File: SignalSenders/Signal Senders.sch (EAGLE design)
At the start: 14 parts, among them IC2 MEGA8-P

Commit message: add reset switch, add power input capacitor
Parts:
- added C3: 22pF, rcl:C-USC0805
- added S1: (no value), SparkFun-Electromechanical:TAC_SWITCHPTH
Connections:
- new net N$1: IC2.PC6(/RESET), S1.4
- net +5V: now also C3.1
- net GND: now also C3.2, S1.2
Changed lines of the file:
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@@
 <layer number="106" name="bPlate" color="7" fill="1" visible="no" active="yes"/>
 <layer number="107" name="Crop" color="7" fill="1" visible="no" active="yes"/>
+<layer number="108" name="tplace-old" color="10" fill="1" visible="yes" active="yes"/>
+<layer number="109" name="ref-old" color="11" fill="1" visible="yes" active="yes"/>
 <layer number="116" name="Patch_BOT" color="9" fill="4" visible="no" active="yes"/>
 <layer number="121" name="_tsilk" color="7" fill="1" visible="no" active="yes"/>
@@
 <layer number="144" name="Drill_legend" color="7" fill="1" visible="no" active="yes"/>
 <layer number="151" name="HeatSink" color="7" fill="1" visible="no" active="yes"/>
+<layer number="199" name="Contour" color="7" fill="1" visible="yes" active="yes"/>
 <layer number="200" name="200bmp" color="1" fill="10" visible="no" active="yes"/>
 <layer number="201" name="201bmp" color="2" fill="10" visible="no" active="yes"/>
@@
 <part name="FRAME1" library="frames" deviceset="A4L-LOC" device=""/>
 <part name="Y1" library="SparkFun-FreqCtrl" deviceset="CRYSTAL" device="HC49US"/>
+<part name="S1" library="SparkFun-Electromechanical" deviceset="TAC_SWITCH" device="PTH"/>
+<part name="GND9" library="supply1" deviceset="GND" device=""/>
+<part name="GND10" library="supply1" deviceset="GND" device=""/>
+<part name="C3" library="rcl" deviceset="C-US" device="C0805" value="22pF"/>
 </parts>
 <sheets>
@@
 <instance part="FRAME1" gate="G$1" x="25.4" y="-40.64"/>
 <instance part="Y1" gate="G$1" x="88.9" y="53.34" rot="R90"/>
+<instance part="S1" gate="S" x="121.92" y="73.66"/>
+<instance part="GND9" gate="1" x="111.76" y="68.58"/>
+<instance part="GND10" gate="1" x="121.92" y="20.32"/>
+<instance part="C3" gate="G$1" x="121.92" y="27.94"/>
 </instances>
 <busses>
@@
 <pinref part="P+2" gate="1" pin="+5V"/>
 <wire x1="127" y1="35.56" x2="121.92" y2="35.56" width="0.1524" layer="91"/>
+<pinref part="C3" gate="G$1" pin="1"/>
+<wire x1="121.92" y1="30.48" x2="121.92" y2="35.56" width="0.1524" layer="91"/>
 </segment>
 <segment>
@@
 <pinref part="JP2" gate="A" pin="3"/>
 <wire x1="63.5" y1="17.78" x2="63.5" y2="22.86" width="0.1524" layer="91"/>
+</segment>
+<segment>
+<pinref part="S1" gate="S" pin="2"/>
+<wire x1="116.84" y1="71.12" x2="111.76" y2="71.12" width="0.1524" layer="91"/>
+<pinref part="GND9" gate="1" pin="GND"/>
+</segment>
+<segment>
+<pinref part="GND10" gate="1" pin="GND"/>
+<pinref part="C3" gate="G$1" pin="2"/>
 </segment>
 </net>
@@
 <segment>
 <pinref part="IC2" gate="G$1" pin="PC5(ADC5/SCL)"/>
-<wire x1="175.26" y1="58.42" x2="177.8" y2="58.42" width="0.1524" layer="91"/>
-<wire x1="190.5" y1="58.42" x2="177.8" y2="58.42" width="0.1524" layer="91"/>
 <label x="177.8" y="58.42" size="1.778" layer="95"/>
-</segment>
-<segment>
+<wire x1="175.26" y1="58.42" x2="208.28" y2="58.42" width="0.1524" layer="91"/>
 <pinref part="LED4" gate="G$1" pin="A"/>
 <wire x1="226.06" y1="60.96" x2="208.28" y2="60.96" width="0.1524" layer="91"/>
 <label x="208.28" y="60.96" size="1.778" layer="95"/>
+<wire x1="208.28" y1="58.42" x2="208.28" y2="60.96" width="0.1524" layer="91"/>
 </segment>
 </net>
@@
 <segment>
 <pinref part="IC2" gate="G$1" pin="PC4(ADC4/SDA)"/>
-<wire x1="175.26" y1="60.96" x2="190.5" y2="60.96" width="0.1524" layer="91"/>
 <label x="177.8" y="60.96" size="1.778" layer="95"/>
-</segment>
-<segment>
+<wire x1="175.26" y1="60.96" x2="205.74" y2="60.96" width="0.1524" layer="91"/>
+<wire x1="205.74" y1="60.96" x2="205.74" y2="76.2" width="0.1524" layer="91"/>
 <pinref part="LED3" gate="G$1" pin="A"/>
-<wire x1="226.06" y1="76.2" x2="208.28" y2="76.2" width="0.1524" layer="91"/>
+<wire x1="226.06" y1="76.2" x2="205.74" y2="76.2" width="0.1524" layer="91"/>
 <label x="208.28" y="76.2" size="1.778" layer="95"/>
 </segment>
@@
 <segment>
 <pinref part="IC2" gate="G$1" pin="PC3(ADC3)"/>
-<wire x1="175.26" y1="63.5" x2="190.5" y2="63.5" width="0.1524" layer="91"/>
+<wire x1="175.26" y1="63.5" x2="203.2" y2="63.5" width="0.1524" layer="91"/>
 <label x="177.8" y="63.5" size="1.778" layer="95"/>
-</segment>
-<segment>
+<wire x1="203.2" y1="63.5" x2="203.2" y2="88.9" width="0.1524" layer="91"/>
 <pinref part="LED2" gate="G$1" pin="A"/>
-<wire x1="226.06" y1="88.9" x2="208.28" y2="88.9" width="0.1524" layer="91"/>
+<wire x1="226.06" y1="88.9" x2="203.2" y2="88.9" width="0.1524" layer="91"/>
 <label x="208.28" y="88.9" size="1.778" layer="95"/>
 </segment>
@@
 <segment>
 <pinref part="IC2" gate="G$1" pin="PC2(ADC2)"/>
-<wire x1="175.26" y1="66.04" x2="190.5" y2="66.04" width="0.1524" layer="91"/>
+<wire x1="175.26" y1="66.04" x2="200.66" y2="66.04" width="0.1524" layer="91"/>
 <label x="177.8" y="66.04" size="1.778" layer="95"/>
-</segment>
-<segment>
+<wire x1="200.66" y1="66.04" x2="200.66" y2="104.14" width="0.1524" layer="91"/>
 <pinref part="LED1" gate="G$1" pin="A"/>
-<wire x1="226.06" y1="104.14" x2="208.28" y2="104.14" width="0.1524" layer="91"/>
+<wire x1="226.06" y1="104.14" x2="200.66" y2="104.14" width="0.1524" layer="91"/>
 <label x="208.28" y="104.14" size="1.778" layer="95"/>
 </segment>
 </net>
+<net name="N$1" class="0">
+<segment>
+<pinref part="IC2" gate="G$1" pin="PC6(/RESET)"/>
+<pinref part="S1" gate="S" pin="4"/>
+</segment>
+</net>

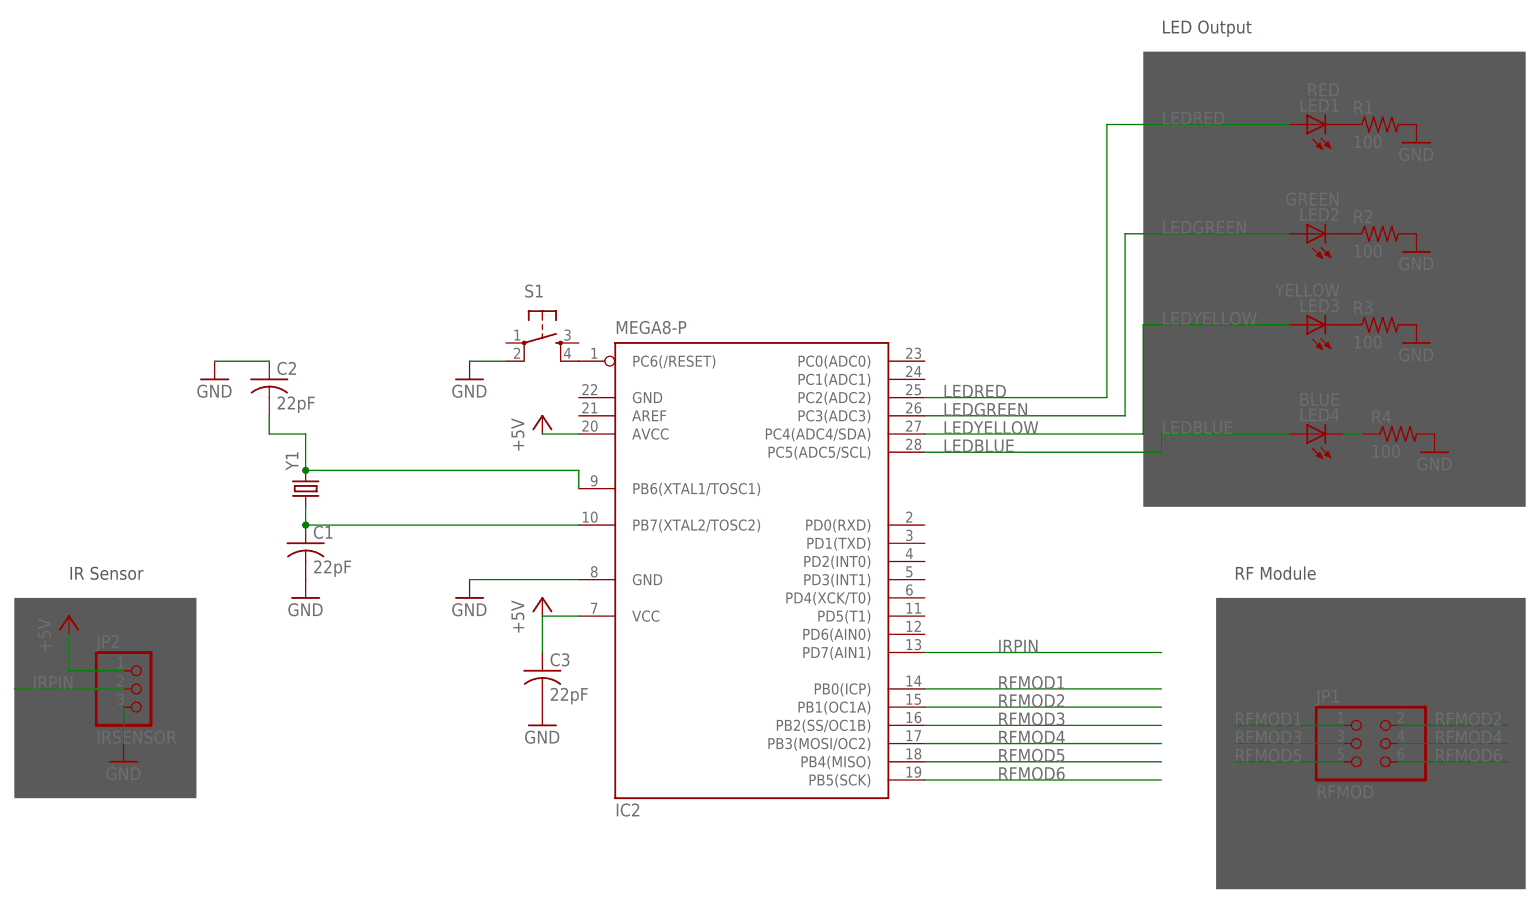
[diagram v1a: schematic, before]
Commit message: untied the lines from chip to LEDs
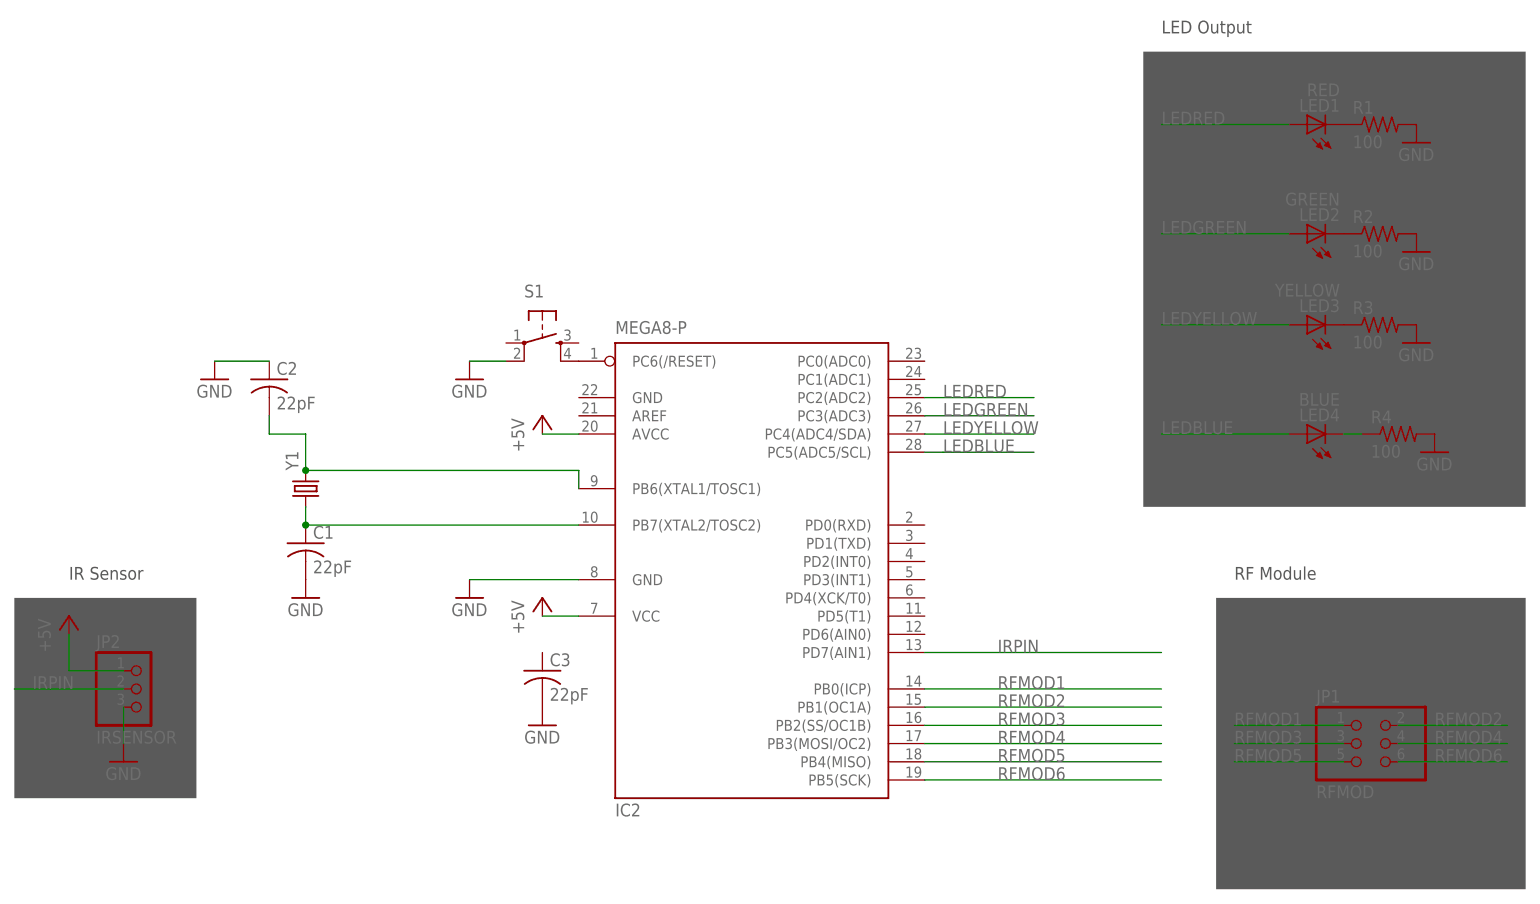
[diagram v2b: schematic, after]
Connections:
- net +5V: no longer C3.1
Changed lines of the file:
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@@
 <pinref part="P+2" gate="1" pin="+5V"/>
 <wire x1="127" y1="35.56" x2="121.92" y2="35.56" width="0.1524" layer="91"/>
-<pinref part="C3" gate="G$1" pin="1"/>
-<wire x1="121.92" y1="30.48" x2="121.92" y2="35.56" width="0.1524" layer="91"/>
 </segment>
 <segment>
@@
 <segment>
 <pinref part="IC2" gate="G$1" pin="PC5(ADC5/SCL)"/>
+<wire x1="175.26" y1="58.42" x2="177.8" y2="58.42" width="0.1524" layer="91"/>
+<wire x1="190.5" y1="58.42" x2="177.8" y2="58.42" width="0.1524" layer="91"/>
 <label x="177.8" y="58.42" size="1.778" layer="95"/>
-<wire x1="175.26" y1="58.42" x2="208.28" y2="58.42" width="0.1524" layer="91"/>
+</segment>
+<segment>
 <pinref part="LED4" gate="G$1" pin="A"/>
 <wire x1="226.06" y1="60.96" x2="208.28" y2="60.96" width="0.1524" layer="91"/>
 <label x="208.28" y="60.96" size="1.778" layer="95"/>
-<wire x1="208.28" y1="58.42" x2="208.28" y2="60.96" width="0.1524" layer="91"/>
 </segment>
 </net>
@@
 <segment>
 <pinref part="IC2" gate="G$1" pin="PC4(ADC4/SDA)"/>
+<wire x1="175.26" y1="60.96" x2="190.5" y2="60.96" width="0.1524" layer="91"/>
 <label x="177.8" y="60.96" size="1.778" layer="95"/>
-<wire x1="175.26" y1="60.96" x2="205.74" y2="60.96" width="0.1524" layer="91"/>
-<wire x1="205.74" y1="60.96" x2="205.74" y2="76.2" width="0.1524" layer="91"/>
+</segment>
+<segment>
 <pinref part="LED3" gate="G$1" pin="A"/>
-<wire x1="226.06" y1="76.2" x2="205.74" y2="76.2" width="0.1524" layer="91"/>
+<wire x1="226.06" y1="76.2" x2="208.28" y2="76.2" width="0.1524" layer="91"/>
 <label x="208.28" y="76.2" size="1.778" layer="95"/>
 </segment>
@@
 <segment>
 <pinref part="IC2" gate="G$1" pin="PC3(ADC3)"/>
-<wire x1="175.26" y1="63.5" x2="203.2" y2="63.5" width="0.1524" layer="91"/>
+<wire x1="175.26" y1="63.5" x2="190.5" y2="63.5" width="0.1524" layer="91"/>
 <label x="177.8" y="63.5" size="1.778" layer="95"/>
-<wire x1="203.2" y1="63.5" x2="203.2" y2="88.9" width="0.1524" layer="91"/>
+</segment>
+<segment>
 <pinref part="LED2" gate="G$1" pin="A"/>
-<wire x1="226.06" y1="88.9" x2="203.2" y2="88.9" width="0.1524" layer="91"/>
+<wire x1="226.06" y1="88.9" x2="208.28" y2="88.9" width="0.1524" layer="91"/>
 <label x="208.28" y="88.9" size="1.778" layer="95"/>
 </segment>
@@
 <segment>
 <pinref part="IC2" gate="G$1" pin="PC2(ADC2)"/>
-<wire x1="175.26" y1="66.04" x2="200.66" y2="66.04" width="0.1524" layer="91"/>
+<wire x1="175.26" y1="66.04" x2="190.5" y2="66.04" width="0.1524" layer="91"/>
 <label x="177.8" y="66.04" size="1.778" layer="95"/>
-<wire x1="200.66" y1="66.04" x2="200.66" y2="104.14" width="0.1524" layer="91"/>
+</segment>
+<segment>
 <pinref part="LED1" gate="G$1" pin="A"/>
-<wire x1="226.06" y1="104.14" x2="200.66" y2="104.14" width="0.1524" layer="91"/>
+<wire x1="226.06" y1="104.14" x2="208.28" y2="104.14" width="0.1524" layer="91"/>
 <label x="208.28" y="104.14" size="1.778" layer="95"/>
 </segment>

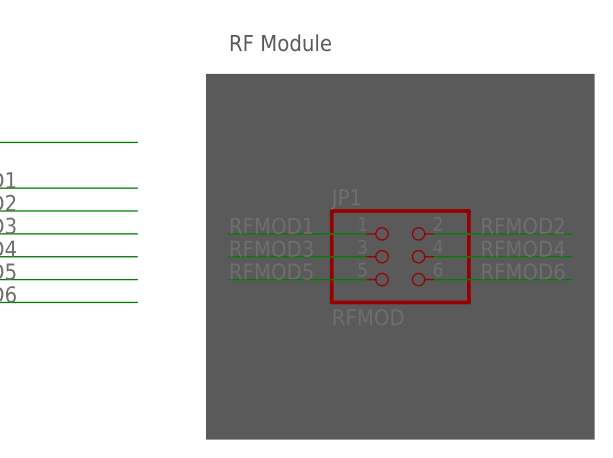
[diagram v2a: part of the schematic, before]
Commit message: EAGLE - upated RF module to 2x4
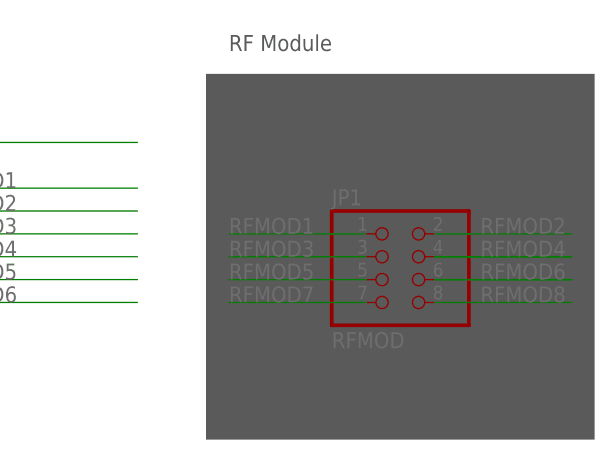
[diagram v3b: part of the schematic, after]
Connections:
- new net RFMOD7: JP1.7
- new net RFMOD8: JP1.8
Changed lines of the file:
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@@
 <?xml version="1.0" encoding="utf-8"?>
 <!DOCTYPE eagle SYSTEM "eagle.dtd">
-<eagle version="6.3">
+<eagle version="6.5.0">
 <drawing>
 <settings>
@@
 <grid distance="0.1" unitdist="inch" unit="inch" style="lines" multiple="1" display="no" altdistance="0.01" altunitdist="inch" altunit="inch"/>
 <layers>
-<layer number="1" name="Top" color="4" fill="1" visible="no" active="no"/>
-<layer number="2" name="Route2" color="1" fill="3" visible="no" active="no"/>
-<layer number="15" name="Route15" color="4" fill="6" visible="no" active="no"/>
-<layer number="16" name="Bottom" color="1" fill="1" visible="no" active="no"/>
-<layer number="17" name="Pads" color="2" fill="1" visible="no" active="no"/>
-<layer number="18" name="Vias" color="2" fill="1" visible="no" active="no"/>
-<layer number="19" name="Unrouted" color="6" fill="1" visible="no" active="no"/>
-<layer number="20" name="Dimension" color="15" fill="1" visible="no" active="no"/>
-<layer number="21" name="tPlace" color="7" fill="1" visible="no" active="no"/>
-<layer number="22" name="bPlace" color="7" fill="1" visible="no" active="no"/>
-<layer number="23" name="tOrigins" color="15" fill="1" visible="no" active="no"/>
-<layer number="24" name="bOrigins" color="15" fill="1" visible="no" active="no"/>
-<layer number="25" name="tNames" color="7" fill="1" visible="no" active="no"/>
-<layer number="26" name="bNames" color="7" fill="1" visible="no" active="no"/>
-<layer number="27" name="tValues" color="7" fill="1" visible="no" active="no"/>
-<layer number="28" name="bValues" color="7" fill="1" visible="no" active="no"/>
+<layer number="1" name="Top" color="4" fill="1" visible="yes" active="no"/>
+<layer number="2" name="Route2" color="1" fill="3" visible="yes" active="no"/>
+<layer number="15" name="Route15" color="4" fill="6" visible="yes" active="no"/>
+<layer number="16" name="Bottom" color="1" fill="1" visible="yes" active="no"/>
+<layer number="17" name="Pads" color="2" fill="1" visible="yes" active="no"/>
+<layer number="18" name="Vias" color="2" fill="1" visible="yes" active="no"/>
+<layer number="19" name="Unrouted" color="6" fill="1" visible="yes" active="no"/>
+<layer number="20" name="Dimension" color="15" fill="1" visible="yes" active="no"/>
+<layer number="21" name="tPlace" color="7" fill="1" visible="yes" active="no"/>
+<layer number="22" name="bPlace" color="7" fill="1" visible="yes" active="no"/>
+<layer number="23" name="tOrigins" color="15" fill="1" visible="yes" active="no"/>
+<layer number="24" name="bOrigins" color="15" fill="1" visible="yes" active="no"/>
+<layer number="25" name="tNames" color="7" fill="1" visible="yes" active="no"/>
+<layer number="26" name="bNames" color="7" fill="1" visible="yes" active="no"/>
+<layer number="27" name="tValues" color="7" fill="1" visible="yes" active="no"/>
+<layer number="28" name="bValues" color="7" fill="1" visible="yes" active="no"/>
 <layer number="29" name="tStop" color="7" fill="3" visible="no" active="no"/>
 <layer number="30" name="bStop" color="7" fill="6" visible="no" active="no"/>
@@
 <layer number="35" name="tGlue" color="7" fill="4" visible="no" active="no"/>
 <layer number="36" name="bGlue" color="7" fill="5" visible="no" active="no"/>
-<layer number="37" name="tTest" color="7" fill="1" visible="no" active="no"/>
-<layer number="38" name="bTest" color="7" fill="1" visible="no" active="no"/>
+<layer number="37" name="tTest" color="7" fill="1" visible="yes" active="no"/>
+<layer number="38" name="bTest" color="7" fill="1" visible="yes" active="no"/>
 <layer number="39" name="tKeepout" color="4" fill="11" visible="no" active="no"/>
 <layer number="40" name="bKeepout" color="1" fill="11" visible="no" active="no"/>
@@
 <layer number="44" name="Drills" color="7" fill="1" visible="no" active="no"/>
 <layer number="45" name="Holes" color="7" fill="1" visible="no" active="no"/>
-<layer number="46" name="Milling" color="3" fill="1" visible="no" active="no"/>
-<layer number="47" name="Measures" color="7" fill="1" visible="no" active="no"/>
-<layer number="48" name="Document" color="7" fill="1" visible="no" active="no"/>
-<layer number="49" name="Reference" color="7" fill="1" visible="no" active="no"/>
-<layer number="50" name="dxf" color="7" fill="1" visible="no" active="no"/>
-<layer number="51" name="tDocu" color="6" fill="9" visible="no" active="no"/>
-<layer number="52" name="bDocu" color="7" fill="1" visible="no" active="no"/>
-<layer number="53" name="tGND_GNDA" color="7" fill="9" visible="no" active="no"/>
-<layer number="54" name="bGND_GNDA" color="1" fill="9" visible="no" active="no"/>
-<layer number="56" name="wert" color="7" fill="1" visible="no" active="no"/>
+<layer number="46" name="Milling" color="3" fill="1" visible="yes" active="no"/>
+<layer number="47" name="Measures" color="7" fill="1" visible="yes" active="no"/>
+<layer number="48" name="Document" color="7" fill="1" visible="yes" active="no"/>
+<layer number="49" name="Reference" color="7" fill="1" visible="yes" active="no"/>
+<layer number="50" name="dxf" color="7" fill="1" visible="yes" active="no"/>
+<layer number="51" name="tDocu" color="6" fill="9" visible="yes" active="no"/>
+<layer number="52" name="bDocu" color="7" fill="1" visible="yes" active="no"/>
+<layer number="53" name="tGND_GNDA" color="7" fill="9" visible="yes" active="no"/>
+<layer number="54" name="bGND_GNDA" color="1" fill="9" visible="yes" active="no"/>
+<layer number="56" name="wert" color="7" fill="1" visible="yes" active="no"/>
 <layer number="91" name="Nets" color="2" fill="1" visible="yes" active="yes"/>
 <layer number="92" name="Busses" color="1" fill="1" visible="yes" active="yes"/>
@@
 <label x="246.38" y="17.78" size="1.778" layer="95"/>
 <wire x1="241.3" y1="17.78" x2="256.54" y2="17.78" width="0.1524" layer="91"/>
+<wire x1="241.3" y1="17.78" x2="256.54" y2="17.78" width="0.1524" layer="91"/>
 </segment>
 </net>
@@
 <wire x1="256.54" y1="15.24" x2="241.3" y2="15.24" width="0.1524" layer="91"/>
 <label x="246.38" y="15.24" size="1.778" layer="95"/>
+<wire x1="256.54" y1="15.24" x2="241.3" y2="15.24" width="0.1524" layer="91"/>
 </segment>
 </net>
@@
 </segment>
 </net>
+<net name="RFMOD7" class="0">
+<segment>
+<pinref part="JP1" gate="A" pin="7"/>
+<wire x1="218.44" y1="12.7" x2="233.68" y2="12.7" width="0.1524" layer="91"/>
+<label x="218.44" y="12.7" size="1.778" layer="95"/>
+</segment>
+</net>
+<net name="RFMOD8" class="0">
+<segment>
+<pinref part="JP1" gate="A" pin="8"/>
+<wire x1="241.3" y1="12.7" x2="256.54" y2="12.7" width="0.1524" layer="91"/>
+<label x="246.38" y="12.7" size="1.778" layer="95"/>
+</segment>
+</net>
